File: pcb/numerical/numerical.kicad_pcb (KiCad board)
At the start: 4 copper layers, 76 parts, among them J1 AudioJack3_Ground, U1 Raspberry_Pi_Pico

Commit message: numerical done
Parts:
- removed the D1 at (150.3, 126.0)
- removed the LED1 at (173.0, 84.0)
- removed the R3 at (151.0, 128.9)
- added LED6: LED, MX V2 Misc:MX-LED-PolarityMarked, F.Cu at (143.9, 69.9)
- added R8: R, Resistor_SMD:R_0603_1608Metric_Pad0.98x0.95mm_HandSolder, B.Cu at (137.7, 75.3)
- D1, D11, D12, D13, D16, D17, D18, D2, D21, D22, D23, D3, D4, D5, D7, D8, D9, R1, R10, R11, R13, R14, R15, R18, R19, R2, R20, R23, R24, R25, R3, R4, R5, R6, R7, R9: moved to B.Cu
- moved R23 264.6 mm to (90.1, 189.6), turned to -90 degrees
- moved R18 261.5 mm to (80.5, 170.5), turned to -90 degrees
- moved R13 258.8 mm to (80.5, 151.5), turned to -90 degrees
- moved R3 251.8 mm to (80.5, 132.4), turned to -90 degrees
- moved S22 251.1 mm to (96.3, 184.2)
- moved R19 250.9 mm to (99.6, 170.5), turned to -90 degrees
- moved R4 249.2 mm to (80.5, 113.4), turned to -90 degrees
- moved LED16 245.1 mm to (86.8, 165.2)
- moved R14 239.6 mm to (99.6, 151.5), turned to -90 degrees
- moved D21 239.5 mm to (102.4, 189.0), turned to 90 degrees
- moved R24 237.1 mm to (118.6, 189.6), turned to -90 degrees
- moved D16 234.0 mm to (92.8, 169.9), turned to 90 degrees
- moved S17 232.5 mm to (86.8, 165.2)
- moved R20 232.1 mm to (118.6, 170.5), turned to -90 degrees
- moved D11 231.7 mm to (92.8, 150.9), turned to 90 degrees
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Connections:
- R4 pad 2: Net-(R4-Pad2) -> GND
- R5 pad 2: Net-(R4-Pad2) -> GND
- R6 pad 2: Net-(R4-Pad2) -> GND
- R7 pad 2: Net-(R4-Pad2) -> GND
- S12 pad 1: Collumn2 -> Collumn1
- S13 pad 1: Collumn3 -> Collumn2
- S14 pad 1: Collumn4 -> Collumn3
- S17 pad 1: Collumn2 -> Collumn1
- S18 pad 1: Collumn3 -> Collumn2
- S19 pad 1: Collumn4 -> Collumn3
- S22 pad 1: Collumn2 -> Collumn1
- U1 pad 10: Collumn2 -> Row4
- U1 pad 11: Collumn3 -> Row3
- U1 pad 12: Collumn4 -> Row2
- U1 pad 14: unconnected-(U1-GPIO10-Pad14) -> Row1
- U1 pad 15: Row1 -> unconnected-(U1-GPIO11-Pad15)
- U1 pad 16: Row2 -> Collumn4
- U1 pad 17: Row3 -> Collumn3
- U1 pad 19: Row4 -> Collumn2
- U1 pad 20: Row5 -> Collumn1
- U1 pad 9: Collumn1 -> Row5
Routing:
- net GND: track 0.00 -> 708.7 mm, vias 0 -> 18
- net +5V: track 0.00 -> 540.3 mm, vias 0 -> 21
- net Row5: track 0.00 -> 229.1 mm, vias 0 -> 3
- net Row4: track 0.00 -> 188.7 mm, vias 0 -> 3
- net Row3: track 0.00 -> 176.9 mm, vias 0 -> 4
- net Row2: track 0.00 -> 173.4 mm, vias 0 -> 4
- net Row1: track 0.00 -> 133.0 mm, vias 0 -> 4
- net Collumn1: track 0.00 -> 126.5 mm
- net Collumn4: track 0.00 -> 111.9 mm, vias 0 -> 2
- net Collumn3: track 0.00 -> 106.5 mm
- net Net-(U1-RUN): track 0.00 -> 91.3 mm, vias 0 -> 2
- net Collumn2: track 0.00 -> 86.4 mm
- net Net-(U1-GPIO4): track 0.00 -> 71.2 mm, vias 0 -> 3
- net Net-(U1-GPIO5): track 0.00 -> 60.4 mm
- net Net-(U1-3V3): track 0.00 -> 19.2 mm
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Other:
- board outline added: 88.6 x 167.9 mm
- copper layers 4 -> 2

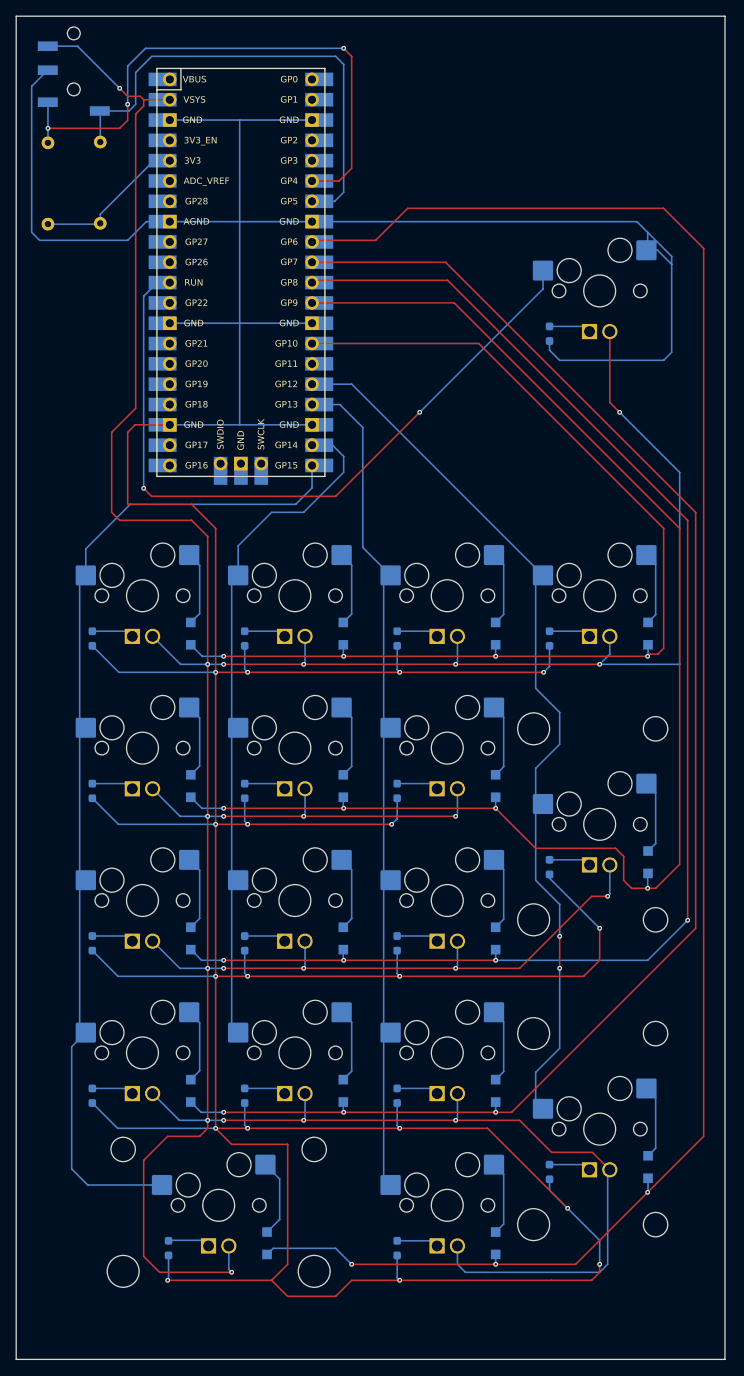
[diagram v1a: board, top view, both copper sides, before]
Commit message: added copper zone fills
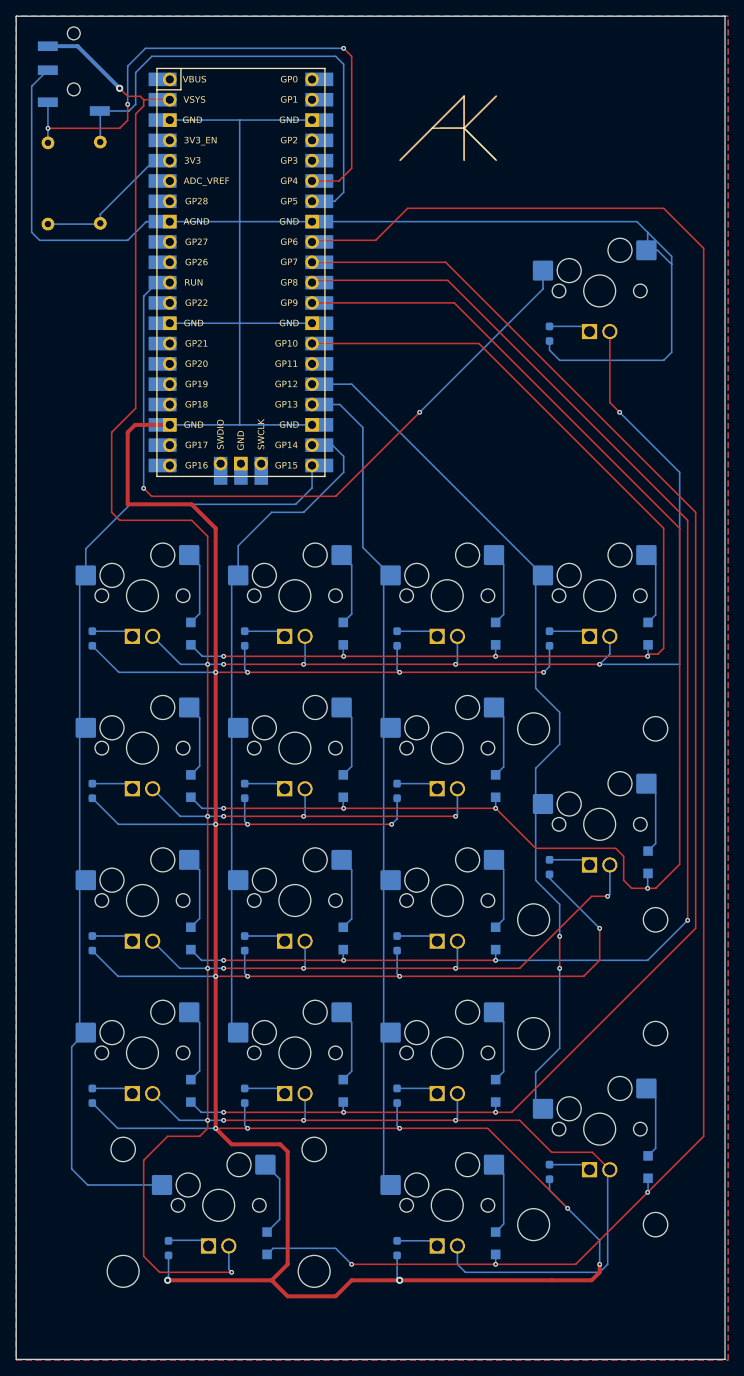
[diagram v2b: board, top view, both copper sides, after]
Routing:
- net (no net): track 0.00 -> 67.3 mm
- net GND: track 708.7 -> 708.1 mm
- added copper zone on F.Cu, net +5V
- added copper zone on B.Cu, net GND

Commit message: gerber files
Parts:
- added REF**: MountingHole_2.2mm_M2, MountingHole:MountingHole_2.2mm_M2, F.Cu at (156.0, 199.6)
- added REF**: MountingHole_2.2mm_M2, MountingHole:MountingHole_2.2mm_M2, F.Cu at (75.0, 68.6)
- added REF**: MountingHole_2.2mm_M2, MountingHole:MountingHole_2.2mm_M2, F.Cu at (75.0, 199.6)
- added REF**: MountingHole_2.2mm_M2, MountingHole:MountingHole_2.2mm_M2, F.Cu at (144.0, 123.6)
- added REF**: MountingHole_2.2mm_M2, MountingHole:MountingHole_2.2mm_M2, F.Cu at (156.0, 39.6)
